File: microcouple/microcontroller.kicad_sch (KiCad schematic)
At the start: 0 parts

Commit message: Add decoupling caps on MCU
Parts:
- added C2, C3, C4, C5, C6, C7: 100nF, Capacitor_SMD:C_0805_2012Metric_Pad1.18x1.45mm_HandSolder, symbol Device:C
- added FB1: 120R @ 100MHz, Inductor_SMD:L_0805_2012Metric_Pad1.15x1.40mm_HandSolder, symbol Device:FerriteBead
- added U1: STM32F070RBTx, Package_QFP:LQFP-64_10x10mm_P0.5mm, symbol MCU_ST_STM32F0:STM32F070RBTx
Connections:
- new net +3.3V: C2.1, C3.1, C4.1, C5.1, C6.1, FB1.1, U1.1 (VDD), U1.19 (VDD), U1.32 (VDD), U1.48 (VDD), U1.64 (VDD)
- new net +3.3VA: C7.1, FB1.2, U1.13 (VDDA)
- new net GND: C2.2, C3.2, C4.2, C5.2, C6.2, C7.2, U1.12 (VSSA), U1.18 (VSS), U1.31 (VSS), U1.47 (VSS), U1.63 (VSS)

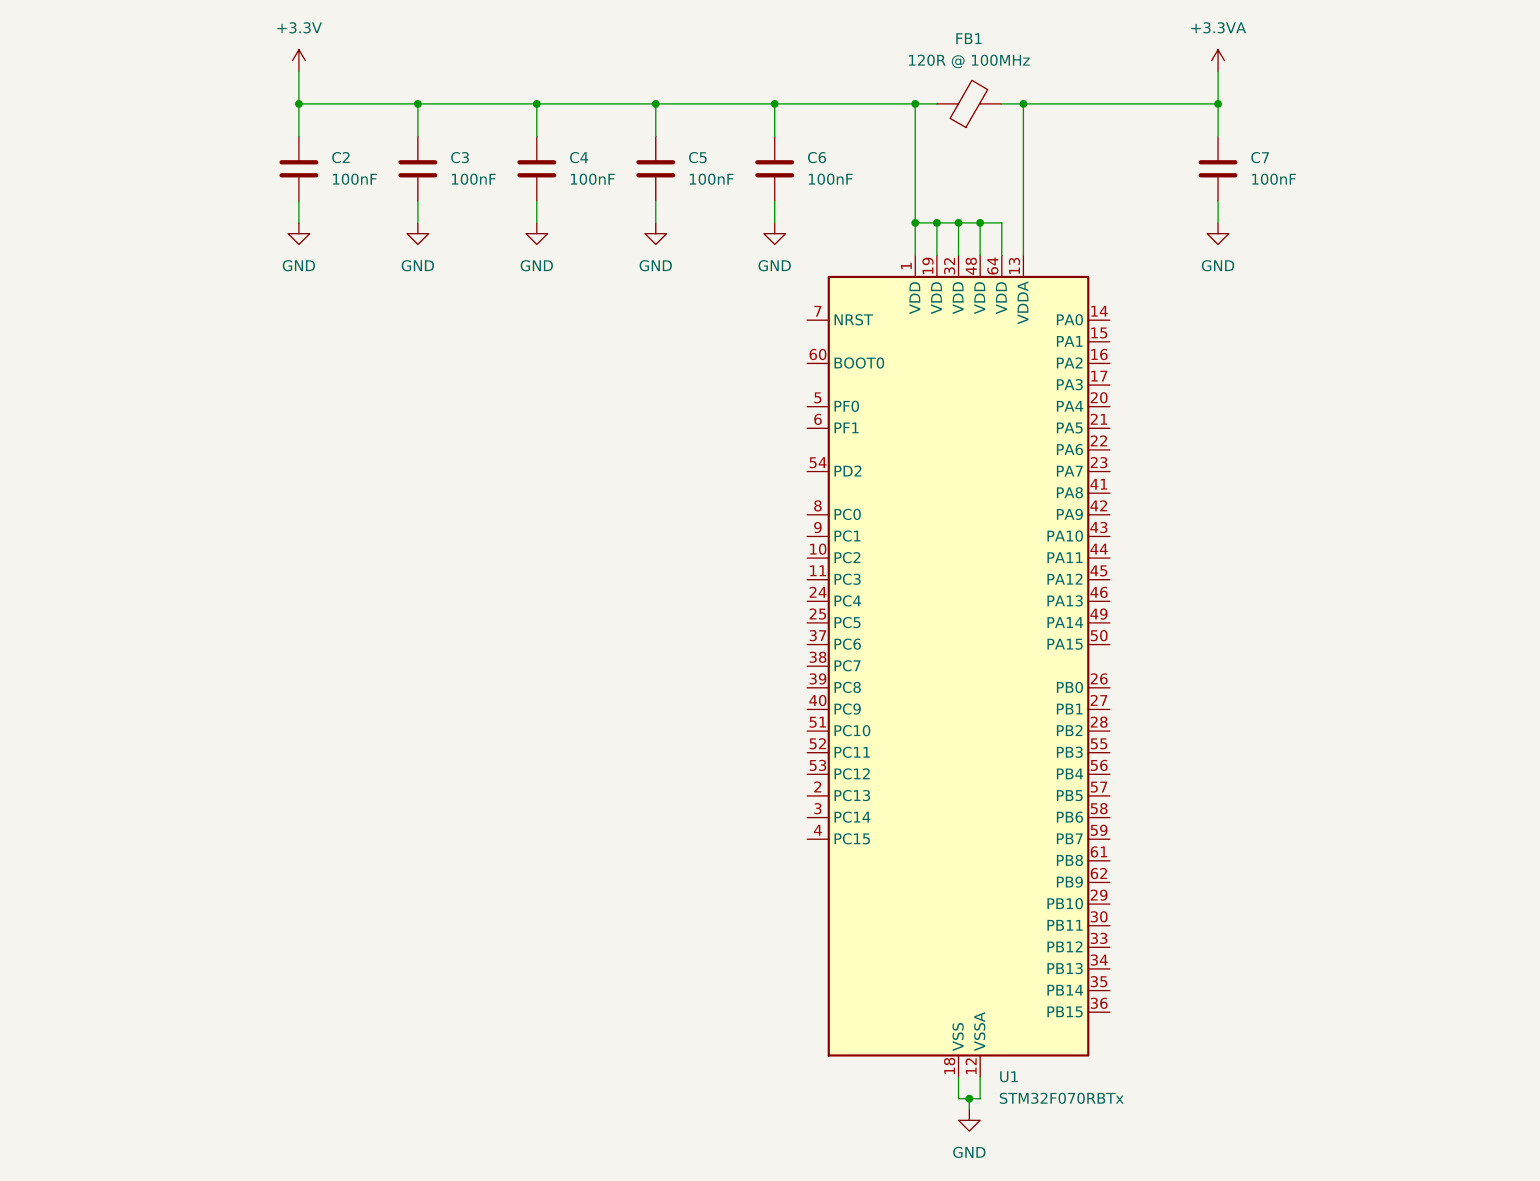
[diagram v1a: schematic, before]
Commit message: Sketch out IR transceiver
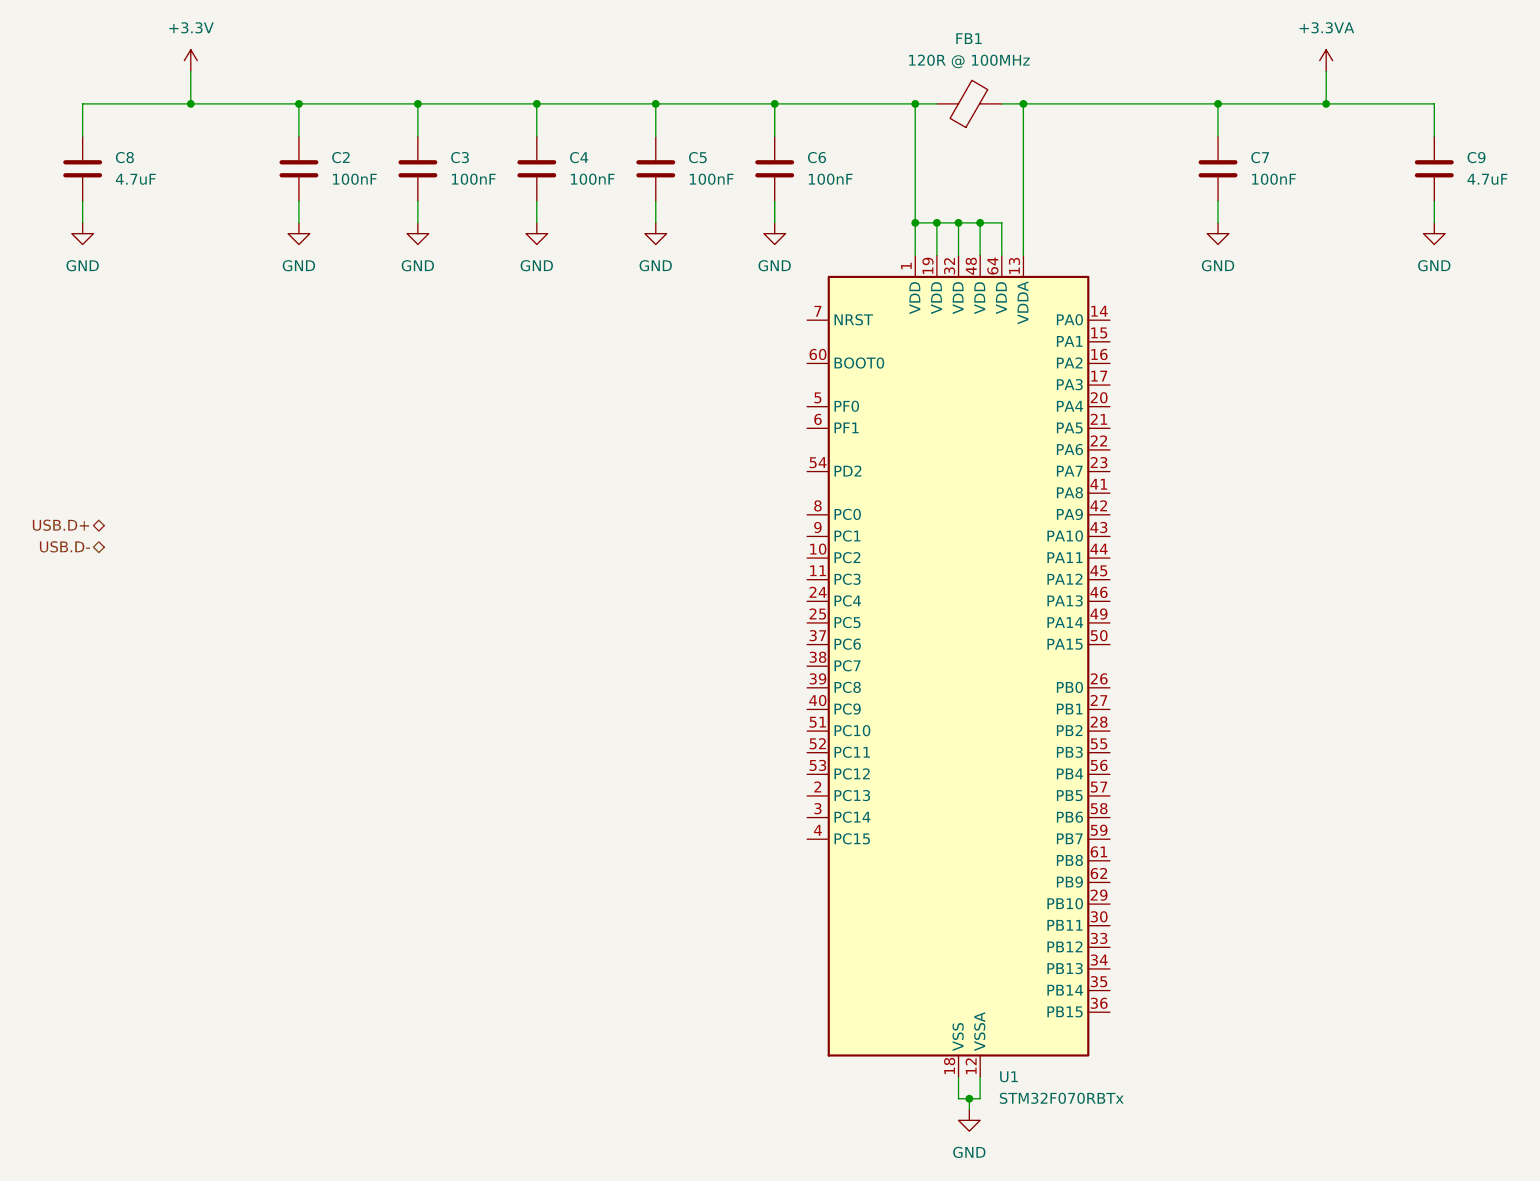
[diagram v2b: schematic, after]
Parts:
- added C8, C9: 4.7uF, Capacitor_SMD:C_0805_2012Metric_Pad1.18x1.45mm_HandSolder, symbol Device:C
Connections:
- net +3.3V: now also C8.1
- net +3.3VA: now also C9.1
- net GND: now also C8.2, C9.2
